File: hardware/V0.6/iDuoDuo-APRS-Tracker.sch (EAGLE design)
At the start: 41 parts, among them IC1 ATMEGA328, IC2 VHF-MODULE, Q2 SI2301, Q3 SI2301, Q4 SI2302, Q5 SI2302, U1 MCP73831, X1 SMA_ANT, Y1 16MHz

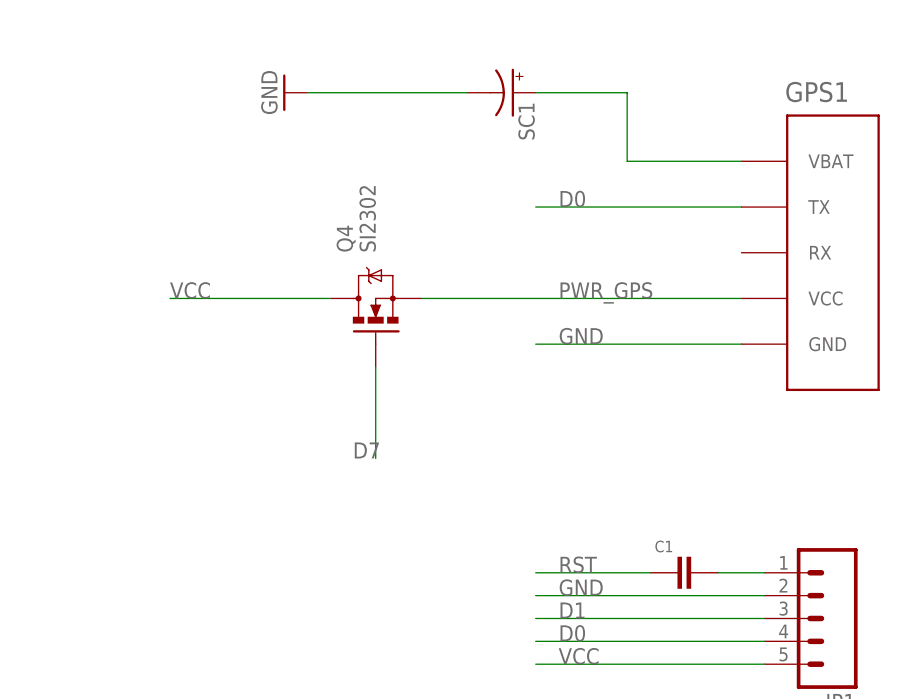
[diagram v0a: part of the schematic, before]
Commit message: hardware: fix the gps switch bug of v0.6
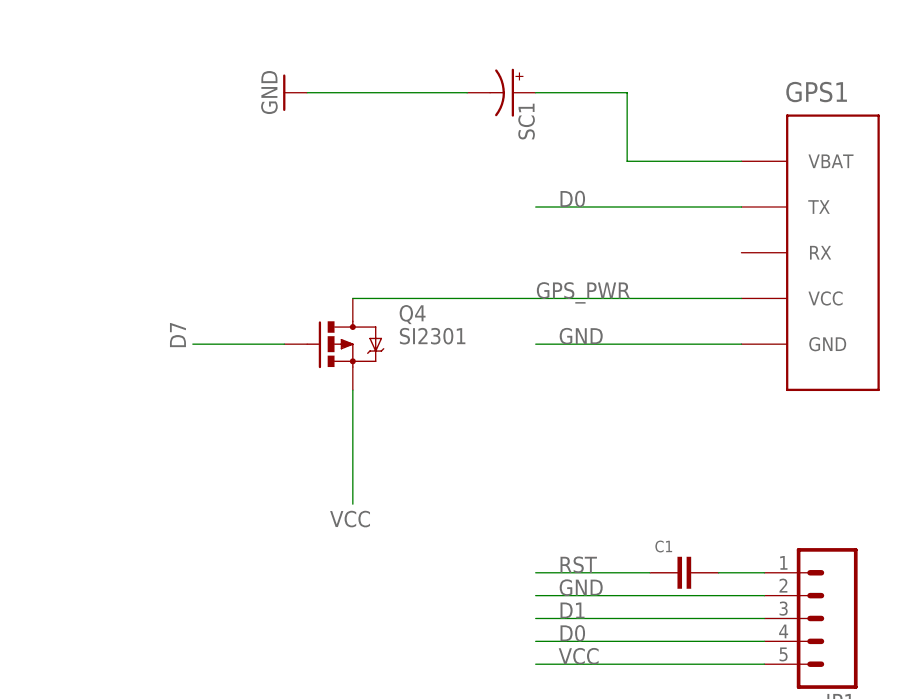
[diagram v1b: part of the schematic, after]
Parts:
- Q4: value SI2302 -> SI2301; device ehl:MOSFET-N-SMD -> ehl:MOSFET-P-SOT23
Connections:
- removed net PWR_GPS: GPS1.VCC, Q4.S
- new net GPS_PWR: GPS1.VCC, Q4.D
- net VCC: now also Q4.S; no longer Q4.D
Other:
- moved on the sheet: Q4
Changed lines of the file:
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@@
 <layer number="59" name="tCarbon" color="7" fill="1" visible="no" active="no"/>
 <layer number="60" name="bCarbon" color="7" fill="1" visible="no" active="no"/>
+<layer number="88" name="SimResults" color="9" fill="1" visible="yes" active="yes"/>
+<layer number="89" name="SimProbes" color="9" fill="1" visible="yes" active="yes"/>
 <layer number="90" name="Modules" color="7" fill="1" visible="yes" active="yes"/>
 <layer number="91" name="Nets" color="2" fill="1" visible="yes" active="yes"/>
@@
 <layer number="113" name="WhiteOver" color="0" fill="1" visible="yes" active="yes"/>
 <layer number="114" name="BlackOver" color="15" fill="1" visible="yes" active="yes"/>
+<layer number="115" name="FRNTMAAT2" color="7" fill="1" visible="yes" active="yes"/>
 <layer number="116" name="Patch_BOT" color="9" fill="4" visible="no" active="yes"/>
+<layer number="117" name="BACKMAAT1" color="7" fill="1" visible="yes" active="yes"/>
 <layer number="118" name="Rect_Pads" color="7" fill="1" visible="yes" active="yes"/>
+<layer number="119" name="KAP_TEKEN" color="7" fill="1" visible="yes" active="yes"/>
+<layer number="120" name="KAP_MAAT1" color="7" fill="1" visible="yes" active="yes"/>
 <layer number="121" name="_tsilk" color="7" fill="1" visible="no" active="yes"/>
 <layer number="122" name="_bsilk" color="7" fill="1" visible="no" active="yes"/>
@@
 <layer number="128" name="_bValues" color="7" fill="1" visible="yes" active="yes"/>
 <layer number="129" name="Mask" color="7" fill="1" visible="yes" active="yes"/>
+<layer number="130" name="SMDSTROOK" color="7" fill="1" visible="yes" active="yes"/>
 <layer number="131" name="prix" color="7" fill="1" visible="no" active="yes"/>
 <layer number="132" name="test" color="7" fill="1" visible="no" active="yes"/>
+<layer number="133" name="bottom_silk" color="7" fill="1" visible="yes" active="yes"/>
+<layer number="134" name="silk_top" color="7" fill="1" visible="yes" active="yes"/>
+<layer number="135" name="silk_bottom" color="7" fill="1" visible="yes" active="yes"/>
+<layer number="136" name="silktop" color="7" fill="1" visible="yes" active="yes"/>
+<layer number="137" name="silkbottom" color="7" fill="1" visible="yes" active="yes"/>
 <layer number="144" name="Drill_legend" color="7" fill="1" visible="no" active="yes"/>
+<layer number="145" name="DrillLegend_01-16" color="7" fill="1" visible="yes" active="yes"/>
+<layer number="146" name="DrillLegend_01-20" color="7" fill="1" visible="yes" active="yes"/>
 <layer number="150" name="Notes" color="7" fill="1" visible="yes" active="yes"/>
 <layer number="151" name="HeatSink" color="7" fill="1" visible="no" active="yes"/>
@@
 <part name="GND10" library="digital-toy" deviceset="GND" device=""/>
 <part name="Q3" library="ehl" deviceset="MOSFET-P" device="-SOT23" value="SI2301"/>
-<part name="Q4" library="ehl" deviceset="MOSFET-N" device="-SMD" value="SI2302"/>
+<part name="Q4" library="ehl" deviceset="MOSFET-P" device="-SOT23" value="SI2301"/>
 <part name="R10" library="ehl" deviceset="0603-RESISTOR" device="" value="1M"/>
 <part name="D3" library="ehl" deviceset="DIODE" device="SOD"/>
@@
 <instance part="GND10" gate="1" x="139.7" y="73.66"/>
 <instance part="Q3" gate="G$1" x="193.04" y="104.14" rot="MR90"/>
-<instance part="Q4" gate="G$1" x="271.78" y="86.36" rot="R90"/>
+<instance part="Q4" gate="G$1" x="269.24" y="81.28"/>
 <instance part="R10" gate="G$1" x="185.42" y="93.98" rot="R180"/>
 <instance part="D3" gate="G$1" x="185.42" y="78.74" rot="R180"/>
@@
 </segment>
 <segment>
-<pinref part="Q4" gate="G$1" pin="D"/>
-<wire x1="266.7" y1="86.36" x2="248.92" y2="86.36" width="0.1524" layer="91"/>
-<label x="248.92" y="86.36" size="1.778" layer="95"/>
-</segment>
-<segment>
 <pinref part="Q3" gate="G$1" pin="D"/>
 <wire x1="198.12" y1="104.14" x2="215.9" y2="104.14" width="0.1524" layer="91"/>
@@
 <wire x1="314.96" y1="45.72" x2="289.56" y2="45.72" width="0.1524" layer="91"/>
 <label x="292.1" y="45.72" size="1.778" layer="95"/>
+</segment>
+<segment>
+<pinref part="Q4" gate="G$1" pin="S"/>
+<wire x1="269.24" y1="76.2" x2="269.24" y2="63.5" width="0.1524" layer="91"/>
+<label x="266.7" y="60.96" size="1.778" layer="95"/>
 </segment>
 </net>
@@
 <segment>
 <pinref part="Q4" gate="G$1" pin="G"/>
-<wire x1="271.78" y1="78.74" x2="271.78" y2="68.58" width="0.1524" layer="91"/>
-<label x="269.24" y="68.58" size="1.778" layer="95"/>
+<wire x1="261.62" y1="81.28" x2="251.46" y2="81.28" width="0.1524" layer="91"/>
+<label x="248.92" y="83.82" size="1.778" layer="95" rot="R270"/>
 </segment>
 </net>
@@
 </segment>
 </net>
-<net name="PWR_GPS" class="0">
-<segment>
-<pinref part="GPS1" gate="G$1" pin="VCC"/>
-<wire x1="312.42" y1="86.36" x2="276.86" y2="86.36" width="0.1524" layer="91"/>
-<label x="292.1" y="86.36" size="1.778" layer="95"/>
-<pinref part="Q4" gate="G$1" pin="S"/>
-</segment>
-</net>
 <net name="VIN" class="0">
 <segment>
@@
 </segment>
 </net>
+<net name="GPS_PWR" class="0">
+<segment>
+<pinref part="GPS1" gate="G$1" pin="VCC"/>
+<pinref part="Q4" gate="G$1" pin="D"/>
+<wire x1="312.42" y1="86.36" x2="269.24" y2="86.36" width="0.1524" layer="91"/>
+<label x="289.56" y="86.36" size="1.778" layer="95"/>
+</segment>
+</net>
